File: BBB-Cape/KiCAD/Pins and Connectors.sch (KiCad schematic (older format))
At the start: 23 parts, among them J1 01x06_Stackable Header, P8 02x23_Stackable Header, P9 02x23_Stackable Header

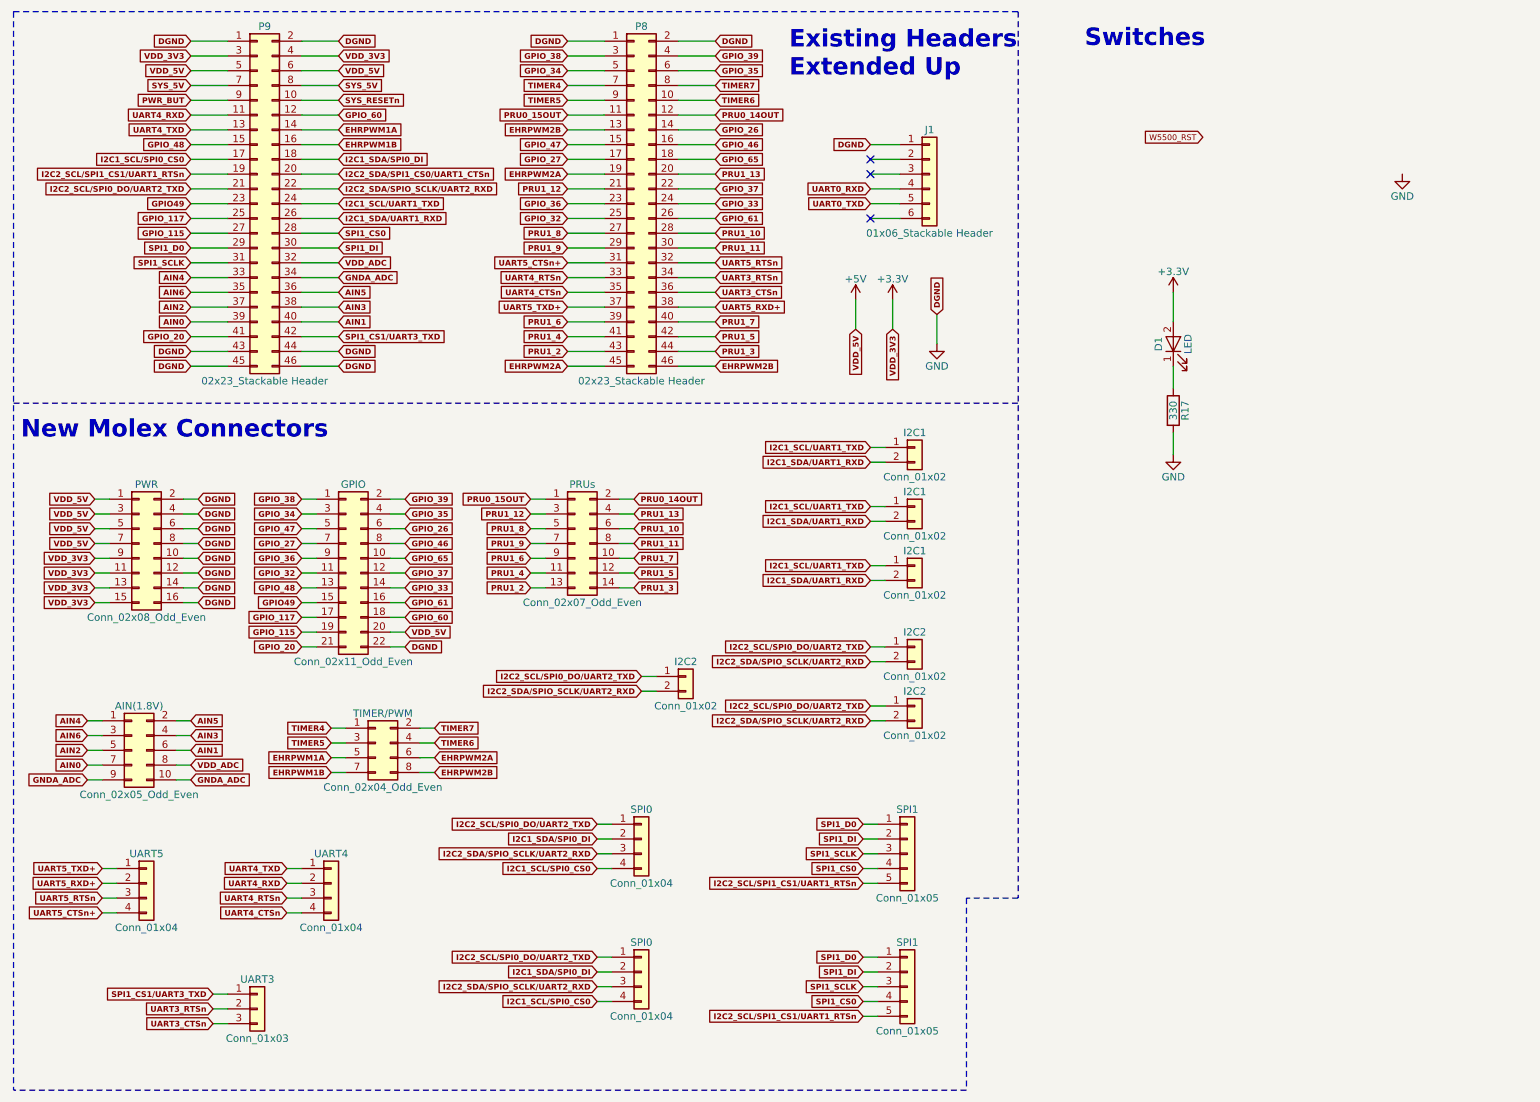
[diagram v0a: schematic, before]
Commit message: layout reorganzied, before SMD molex
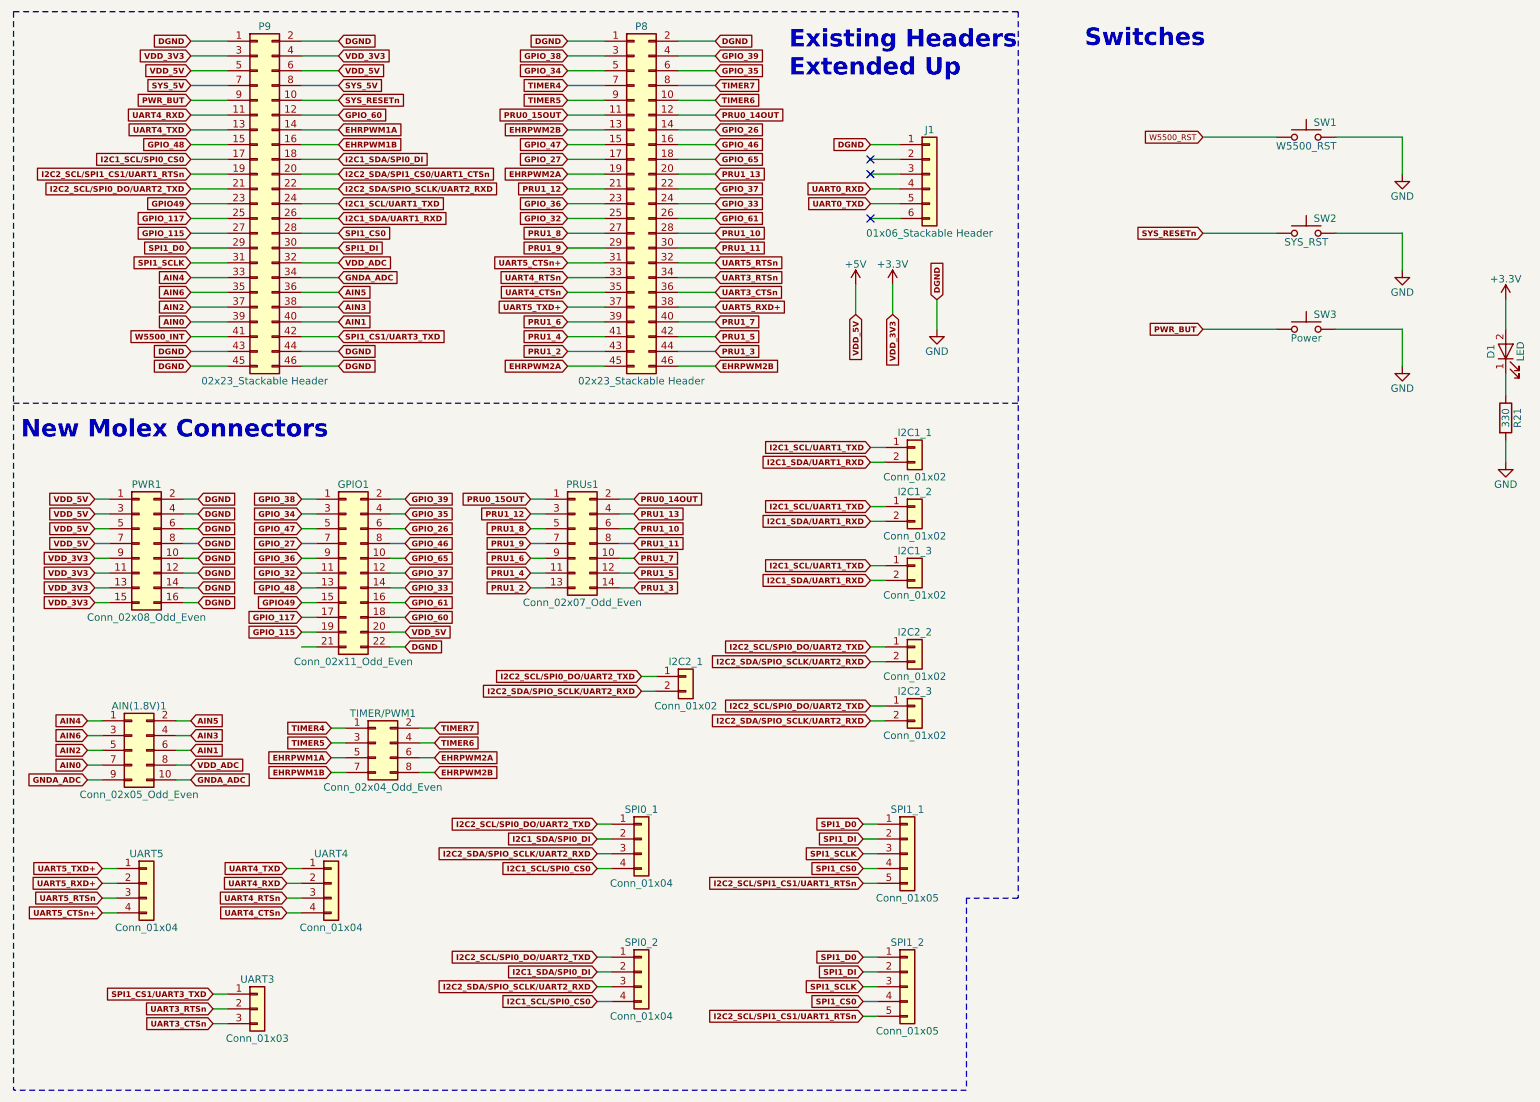
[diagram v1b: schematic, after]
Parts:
- added SW1: W5500_RST, Buttons_Switches_SMD:SW_SPST_B3U-1000P, symbol SW_Push
- added SW2: SYS_RST, Buttons_Switches_SMD:SW_SPST_B3U-1000P, symbol SW_Push
- added SW3: Power, Buttons_Switches_SMD:SW_SPST_B3U-1000P, symbol SW_Push
- renumbered AIN(1.8V) to AIN(1.8V)1, GPIO to GPIO1, I2C1 to I2C1_1, I2C1 to I2C1_2, I2C1 to I2C1_3, I2C2 to I2C2_1, I2C2 to I2C2_2, I2C2 to I2C2_3, PRUs to PRUs1, PWR to PWR1, R17 to R21, SPI0 to SPI0_1, SPI0 to SPI0_2, SPI1 to SPI1_1, SPI1 to SPI1_2, TIMER/PWM to TIMER/PWM1
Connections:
- net GND: now also SW1.2, SW2.2, SW3.2
- net PWR_BUT: now also SW3.1
- net SYS_RESETn: now also SW2.1
- net W5500_RST: now also SW1.1
- net GPIO_20: no longer names the net of GPIO1.21 (Pin_21)
- net GPIO_20: no longer P9.41 (Pin_41)
- new net W5500_INT: P9.41 (Pin_41)
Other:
- moved on the sheet: D1, R21

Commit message: Rev1 Board Post for Checkup
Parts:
- removed I2C1_2, I2C1_3, I2C2_1, I2C2_3: Conn_01x02, Pin_Headers:Pin_Header_Straight_1x02_Pitch2.54mm, symbol Conn_01x02
- removed SPI0_2: Conn_01x04, Pin_Headers:Pin_Header_Straight_1x04_Pitch2.54mm, symbol Conn_01x04
- removed SPI1_2: Conn_01x05, Pin_Headers:Pin_Header_Straight_1x05_Pitch2.54mm, symbol Conn_01x05
- AIN(1.8V)1: footprint Pin_Headers:Pin_Header_Straight_2x05_Pitch2.54mm -> Pin_Headers:Pin_Header_Straight_2x05_Pitch2.54mm_SMD
- GPIO1: footprint Pin_Headers:Pin_Header_Straight_2x11_Pitch2.54mm -> Pin_Headers:Pin_Header_Straight_2x11_Pitch2.54mm_SMD
- I2C1_0: renamed from I2C1_1; footprint Pin_Headers:Pin_Header_Straight_1x02_Pitch2.54mm -> Pin_Headers:Pin_Header_Straight_1x02_Pitch2.54mm_SMD_Pin1Left
- I2C2_0: renamed from I2C2_2; footprint Pin_Headers:Pin_Header_Straight_1x02_Pitch2.54mm -> Pin_Headers:Pin_Header_Straight_1x02_Pitch2.54mm_SMD_Pin1Left
- PRUs1: footprint Pin_Headers:Pin_Header_Straight_2x07_Pitch2.54mm -> Pin_Headers:Pin_Header_Straight_2x07_Pitch2.54mm_SMD
- PWR1: footprint Pin_Headers:Pin_Header_Straight_2x08_Pitch2.54mm -> Pin_Headers:Pin_Header_Straight_2x08_Pitch2.54mm_SMD
- SPI0_1, UART4, UART5: footprint Pin_Headers:Pin_Header_Straight_1x04_Pitch2.54mm -> Pin_Headers:Pin_Header_Straight_1x04_Pitch2.54mm_SMD_Pin1Left
- SPI1_1: footprint Pin_Headers:Pin_Header_Straight_1x05_Pitch2.54mm -> Pin_Headers:Pin_Header_Straight_1x05_Pitch2.54mm_SMD_Pin1Left
- TIMER/PWM1: footprint Pin_Headers:Pin_Header_Straight_2x04_Pitch2.54mm -> Pin_Headers:Pin_Header_Straight_2x04_Pitch2.54mm_SMD
- UART3: footprint Pin_Headers:Pin_Header_Straight_1x03_Pitch2.54mm -> Pin_Headers:Pin_Header_Straight_1x03_Pitch2.54mm_SMD_Pin1Left
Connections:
- net GND: now also GPIO1.21 (Pin_21)
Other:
- moved on the sheet: I2C2_0
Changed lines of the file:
@@
 F 0 "PWR1" H 1400 4500 50  0000 C CNN
 F 1 "Conn_02x08_Odd_Even" H 1400 3600 50  0000 C CNN
-F 2 "Pin_Headers:Pin_Header_Straight_2x08_Pitch2.54mm" H 1350 4100 50  0001 C CNN
+F 2 "Pin_Headers:Pin_Header_Straight_2x08_Pitch2.54mm_SMD" H 1350 4100 50  0001 C CNN
 F 3 "" H 1350 4100 50  0001 C CNN
 	1    1350 4100
@@
 F 0 "TIMER/PWM1" H 3000 5650 50  0000 C CNN
 F 1 "Conn_02x04_Odd_Even" H 3000 5150 50  0000 C CNN
-F 2 "Pin_Headers:Pin_Header_Straight_2x04_Pitch2.54mm" H 2950 5450 50  0001 C CNN
+F 2 "Pin_Headers:Pin_Header_Straight_2x04_Pitch2.54mm_SMD" H 2950 5450 50  0001 C CNN
 F 3 "" H 2950 5450 50  0001 C CNN
 	1    2950 5450
@@
 F 0 "AIN(1.8V)1" H 1350 5800 50  0000 C CNN
 F 1 "Conn_02x05_Odd_Even" H 1350 5200 50  0000 C CNN
-F 2 "Pin_Headers:Pin_Header_Straight_2x05_Pitch2.54mm" H 1300 5500 50  0001 C CNN
+F 2 "Pin_Headers:Pin_Header_Straight_2x05_Pitch2.54mm_SMD" H 1300 5500 50  0001 C CNN
 F 3 "" H 1300 5500 50  0001 C CNN
 	1    1300 5500
@@
 F 0 "GPIO1" H 2800 4900 50  0000 C CNN
 F 1 "Conn_02x11_Odd_Even" H 2800 3700 50  0000 C CNN
-F 2 "Pin_Headers:Pin_Header_Straight_2x11_Pitch2.54mm" H 2750 4300 50  0001 C CNN
+F 2 "Pin_Headers:Pin_Header_Straight_2x11_Pitch2.54mm_SMD" H 2750 4300 50  0001 C CNN
 F 3 "" H 2750 4300 50  0001 C CNN
 	1    2750 4300
@@
 F 0 "PRUs1" H 4350 4500 50  0000 C CNN
 F 1 "Conn_02x07_Odd_Even" H 4350 3700 50  0000 C CNN
-F 2 "Pin_Headers:Pin_Header_Straight_2x07_Pitch2.54mm" H 4300 4100 50  0001 C CNN
+F 2 "Pin_Headers:Pin_Header_Straight_2x07_Pitch2.54mm_SMD" H 4300 4100 50  0001 C CNN
 F 3 "" H 4300 4100 50  0001 C CNN
 	1    4300 4100
@@
 $EndComp
 $Comp
-L Conn_01x02 I2C1_1
+L Conn_01x02 I2C1_0
 U 1 1 5A091929
 P 6600 3450
-F 0 "I2C1_1" H 6600 3550 50  0000 C CNN
+F 0 "I2C1_0" H 6600 3550 50  0000 C CNN
 F 1 "Conn_01x02" H 6600 3250 50  0000 C CNN
-F 2 "Pin_Headers:Pin_Header_Straight_1x02_Pitch2.54mm" H 6600 3450 50  0001 C CNN
+F 2 "Pin_Headers:Pin_Header_Straight_1x02_Pitch2.54mm_SMD_Pin1Left" H 6600 3450 50  0001 C CNN
 F 3 "" H 6600 3450 50  0001 C CNN
 	1    6600 3450
@@
 F 0 "UART3" H 2150 7450 50  0000 C CNN
 F 1 "Conn_01x03" H 2150 7050 50  0000 C CNN
-F 2 "Pin_Headers:Pin_Header_Straight_1x03_Pitch2.54mm" H 2150 7250 50  0001 C CNN
+F 2 "Pin_Headers:Pin_Header_Straight_1x03_Pitch2.54mm_SMD_Pin1Left" H 2150 7250 50  0001 C CNN
 F 3 "" H 2150 7250 50  0001 C CNN
 	1    2150 7250
@@
 F 0 "UART5" H 1400 6600 50  0000 C CNN
 F 1 "Conn_01x04" H 1400 6100 50  0000 C CNN
-F 2 "Pin_Headers:Pin_Header_Straight_1x04_Pitch2.54mm" H 1400 6400 50  0001 C CNN
+F 2 "Pin_Headers:Pin_Header_Straight_1x04_Pitch2.54mm_SMD_Pin1Left" H 1400 6400 50  0001 C CNN
 F 3 "" H 1400 6400 50  0001 C CNN
 	1    1400 6400
@@
 F 0 "SPI0_1" H 4750 6300 50  0000 C CNN
 F 1 "Conn_01x04" H 4750 5800 50  0000 C CNN
-F 2 "Pin_Headers:Pin_Header_Straight_1x04_Pitch2.54mm" H 4750 6100 50  0001 C CNN
+F 2 "Pin_Headers:Pin_Header_Straight_1x04_Pitch2.54mm_SMD_Pin1Left" H 4750 6100 50  0001 C CNN
 F 3 "" H 4750 6100 50  0001 C CNN
 	1    4750 6100
@@
 F 0 "SPI1_1" H 6550 6500 50  0000 C CNN
 F 1 "Conn_01x05" H 6550 5900 50  0000 C CNN
-F 2 "Pin_Headers:Pin_Header_Straight_1x05_Pitch2.54mm" H 6550 6200 50  0001 C CNN
+F 2 "Pin_Headers:Pin_Header_Straight_1x05_Pitch2.54mm_SMD_Pin1Left" H 6550 6200 50  0001 C CNN
 F 3 "" H 6550 6200 50  0001 C CNN
 	1    6550 6200
@@
 $EndComp
 $Comp
-L Conn_01x02 I2C1_2
-U 1 1 5A098726
-P 6600 3850
-F 0 "I2C1_2" H 6600 3950 50  0000 C CNN
-F 1 "Conn_01x02" H 6600 3650 50  0000 C CNN
-F 2 "Pin_Headers:Pin_Header_Straight_1x02_Pitch2.54mm" H 6600 3850 50  0001 C CNN
-F 3 "" H 6600 3850 50  0001 C CNN
-	1    6600 3850
-	1    0    0    -1
-$EndComp
-$Comp
-L Conn_01x02 I2C1_3
-U 1 1 5A098770
-P 6600 4250
-F 0 "I2C1_3" H 6600 4350 50  0000 C CNN
-F 1 "Conn_01x02" H 6600 4050 50  0000 C CNN
-F 2 "Pin_Headers:Pin_Header_Straight_1x02_Pitch2.54mm" H 6600 4250 50  0001 C CNN
-F 3 "" H 6600 4250 50  0001 C CNN
-	1    6600 4250
-	1    0    0    -1
-$EndComp
-$Comp
-L Conn_01x02 I2C2_1
-U 1 1 5A0987C2
-P 5050 5000
-F 0 "I2C2_1" H 5050 5100 50  0000 C CNN
-F 1 "Conn_01x02" H 5050 4800 50  0000 C CNN
-F 2 "Pin_Headers:Pin_Header_Straight_1x02_Pitch2.54mm" H 5050 5000 50  0001 C CNN
-F 3 "" H 5050 5000 50  0001 C CNN
-	1    5050 5000
-	1    0    0    -1
-$EndComp
-$Comp
-L Conn_01x02 I2C2_3
-U 1 1 5A098816
-P 6600 5200
-F 0 "I2C2_3" H 6600 5300 50  0000 C CNN
-F 1 "Conn_01x02" H 6600 5000 50  0000 C CNN
-F 2 "Pin_Headers:Pin_Header_Straight_1x02_Pitch2.54mm" H 6600 5200 50  0001 C CNN
-F 3 "" H 6600 5200 50  0001 C CNN
-	1    6600 5200
-	1    0    0    -1
-$EndComp
-$Comp
-L Conn_01x02 I2C2_2
+L Conn_01x02 I2C2_0
 U 1 1 5A098868
-P 6600 4800
-F 0 "I2C2_2" H 6600 4900 50  0000 C CNN
-F 1 "Conn_01x02" H 6600 4600 50  0000 C CNN
-F 2 "Pin_Headers:Pin_Header_Straight_1x02_Pitch2.54mm" H 6600 4800 50  0001 C CNN
-F 3 "" H 6600 4800 50  0001 C CNN
-	1    6600 4800
-	1    0    0    -1
-$EndComp
-$Comp
-L Conn_01x04 SPI0_2
-U 1 1 5A09907C
-P 4750 7000
-F 0 "SPI0_2" H 4750 7200 50  0000 C CNN
-F 1 "Conn_01x04" H 4750 6700 50  0000 C CNN
-F 2 "Pin_Headers:Pin_Header_Straight_1x04_Pitch2.54mm" H 4750 7000 50  0001 C CNN
-F 3 "" H 4750 7000 50  0001 C CNN
-	1    4750 7000
-	1    0    0    -1
-$EndComp
-$Comp
-L Conn_01x05 SPI1_2
-U 1 1 5A099147
-P 6550 7100
-F 0 "SPI1_2" H 6550 7400 50  0000 C CNN
-F 1 "Conn_01x05" H 6550 6800 50  0000 C CNN
-F 2 "Pin_Headers:Pin_Header_Straight_1x05_Pitch2.54mm" H 6550 7100 50  0001 C CNN
-F 3 "" H 6550 7100 50  0001 C CNN
-	1    6550 7100
+P 6600 4400
+F 0 "I2C2_0" H 6600 4500 50  0000 C CNN
+F 1 "Conn_01x02" H 6600 4200 50  0000 C CNN
+F 2 "Pin_Headers:Pin_Header_Straight_1x02_Pitch2.54mm_SMD_Pin1Left" H 6600 4400 50  0001 C CNN
+F 3 "" H 6600 4400 50  0001 C CNN
+	1    6600 4400
 	1    0    0    -1
 $EndComp
@@
 F 0 "UART4" H 2650 6600 50  0000 C CNN
 F 1 "Conn_01x04" H 2650 6100 50  0000 C CNN
-F 2 "Pin_Headers:Pin_Header_Straight_1x04_Pitch2.54mm" H 2650 6400 50  0001 C CNN
+F 2 "Pin_Headers:Pin_Header_Straight_1x04_Pitch2.54mm_SMD_Pin1Left" H 2650 6400 50  0001 C CNN
 F 3 "" H 2650 6400 50  0001 C CNN
 	1    2650 6400
@@
 	6350 6400 6250 6400
 Wire Wire Line
-	6400 3850 6300 3850
-Wire Wire Line
-	6400 3950 6300 3950
-Wire Wire Line
-	6400 4250 6300 4250
-Wire Wire Line
-	6400 4350 6300 4350
-Wire Wire Line
-	4850 5000 4750 5000
-Wire Wire Line
-	4850 5100 4750 5100
-Wire Wire Line
-	6400 5200 6300 5200
-Wire Wire Line
-	6400 5300 6300 5300
-Wire Wire Line
-	6400 4800 6300 4800
-Wire Wire Line
-	6400 4900 6300 4900
+	6400 4400 6300 4400
+Wire Wire Line
+	6400 4500 6300 4500
 Wire Wire Line
 	4550 6000 4450 6000
@@
 Wire Wire Line
 	4550 6300 4450 6300
-Wire Wire Line
-	4550 6900 4450 6900
-Wire Wire Line
-	4550 7000 4450 7000
-Wire Wire Line
-	4550 7100 4450 7100
-Wire Wire Line
-	4550 7200 4450 7200
-Wire Wire Line
-	6350 6900 6250 6900
-Wire Wire Line
-	6350 7000 6250 7000
-Wire Wire Line
-	6350 7100 6250 7100
-Wire Wire Line
-	6350 7200 6250 7200
-Wire Wire Line
-	6350 7300 6250 7300
 Wire Notes Line
 	7300 6500 6950 6500
@@
 Text GLabel 1850 7150 0    39   Input ~ 8
 SPI1_CS1/UART3_TXD
-Text GLabel 6300 3850 0    39   Input ~ 8
-I2C1_SCL/UART1_TXD
-Text GLabel 6300 3950 0    39   Input ~ 8
-I2C1_SDA/UART1_RXD
 Text GLabel 6300 3450 0    39   Input ~ 8
 I2C1_SCL/UART1_TXD
 Text GLabel 6300 3550 0    39   Input ~ 8
 I2C1_SDA/UART1_RXD
-Text GLabel 6300 4250 0    39   Input ~ 8
-I2C1_SCL/UART1_TXD
-Text GLabel 6300 4350 0    39   Input ~ 8
-I2C1_SDA/UART1_RXD
-Text GLabel 6300 4900 0    39   Input ~ 8
+Text GLabel 6300 4500 0    39   Input ~ 8
 I2C2_SDA/SPIO_SCLK/UART2_RXD
-Text GLabel 6300 4800 0    39   Input ~ 8
+Text GLabel 6300 4400 0    39   Input ~ 8
 I2C2_SCL/SPI0_DO/UART2_TXD
-Text GLabel 6300 5200 0    39   Input ~ 8
-I2C2_SCL/SPI0_DO/UART2_TXD
-Text GLabel 6300 5300 0    39   Input ~ 8
-I2C2_SDA/SPIO_SCLK/UART2_RXD
-Text GLabel 4750 5000 0    39   Input ~ 8
-I2C2_SCL/SPI0_DO/UART2_TXD
-Text GLabel 4750 5100 0    39   Input ~ 8
-I2C2_SDA/SPIO_SCLK/UART2_RXD
 Text GLabel 6250 6000 0    39   Input ~ 8
 SPI1_D0
@@
 Text GLabel 6250 6400 0    39   Input ~ 8
 I2C2_SCL/SPI1_CS1/UART1_RTSn
-Text GLabel 6250 6900 0    39   Input ~ 8
-SPI1_D0
-Text GLabel 6250 7000 0    39   Input ~ 8
-SPI1_DI
-Text GLabel 6250 7100 0    39   Input ~ 8
-SPI1_SCLK
-Text GLabel 6250 7200 0    39   Input ~ 8
-SPI1_CS0
-Text GLabel 6250 7300 0    39   Input ~ 8
-I2C2_SCL/SPI1_CS1/UART1_RTSn
 Text GLabel 4450 6200 0    39   Input ~ 8
 I2C2_SDA/SPIO_SCLK/UART2_RXD
@@
 I2C1_SDA/SPI0_DI
 Text GLabel 4450 6300 0    39   Input ~ 8
-I2C1_SCL/SPI0_CS0
-Text GLabel 4450 6900 0    39   Input ~ 8
-I2C2_SCL/SPI0_DO/UART2_TXD
-Text GLabel 4450 7000 0    39   Input ~ 8
-I2C1_SDA/SPI0_DI
-Text GLabel 4450 7100 0    39   Input ~ 8
-I2C2_SDA/SPIO_SCLK/UART2_RXD
-Text GLabel 4450 7200 0    39   Input ~ 8
 I2C1_SCL/SPI0_CS0
 Wire Wire Line
@@
 Text GLabel 8550 2650 0    39   Input ~ 8
 PWR_BUT
+Text GLabel 2450 4800 0    39   Input ~ 8
+DGND
 $EndSCHEMATC
